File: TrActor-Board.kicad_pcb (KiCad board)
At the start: 6 copper layers, 26 x 50 mm, 125 parts, among them J1 TagConnect, J2 Debug, J3 GCT4720, J4 Batt, J5 NTC, Q1 NMOS, SW1 Power, SW2 Reset, U1 nRF52833_QDxx, U2 DW3210, U3 ICM-40609, U4 ATX-13, U5 nPM1300, U6 USBLC6-2P6, U7 USBLC6-2P6, Y1 32MHz, Y2 32.768k

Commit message: mag added. ready for order?
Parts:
- added C46: 2.2u, Capacitor_SMD:C_0603_1608Metric, F.Cu at (147.1, 99.1)
- added U8: MMC5603NJ, Package_BGA:WLP-4_0.86x0.86mm_P0.4mm, F.Cu at (150.0, 98.5)
- R7, R8: value 10k -> 2.7k
- moved TP29 0.28 mm to (151.5, 83.0)
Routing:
- net SDA: track 23.0 -> 26.1 mm, vias 2 -> 3
- net /BATT_RAW: track 12.7 -> 15.5 mm
- net SCL: track 22.7 -> 25.2 mm, vias 2 -> 3
- net +1V8: track 49.1 -> 50.4 mm, vias 16 -> 18
- net VSYS: track 75.4 -> 76.0 mm
- net GND: track 162.3 -> 162.0 mm, vias 70 -> 134
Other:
- outline, holes or cut-outs redrawn
- board text added: "1V8"
- board text added: "2V5"
- board text added: "BATT"
- board text added: "Batt+"
- board text added: "DW"
- board text added: "Designed by: Nic DeBruin Project TrActor WPI ECE MQP 2026"
- board text added: "EXTON"
- board text added: "GND"
- board text added: "Git Hash: @{vcsidentifier(7)}"
- board text added: "IMU"
- board text added: "INT1-2"
- board text added: "IRQ"
- board text added: "MISO"
- board text added: "MOSI"
- board text added: "NTC+"
- board text added: "PWR"
- board text added: "RST"
- board text added: "RX"
- board text added: "SCL"
- board text added: "SDA"
- board text added: "SYNC"
- board text added: "TO:DO: - funny silkscreen - version tracking - JLCPCB serial number thing"
- board text added: "TX"
- board text added: "TrActor."
- board text added: "VBUS"
- board text added: "VPRE"
- board text added: "VSYS"
- board text added: "WAKE"
- board text removed: "#are we actually using these lol?"
- board text removed: "PLACEHOLDER, THIS THING IS ASS"
- board text removed: "TO:DO: - Figure out actually good NFC antenna & place - layout nPM - finalize LED positions - locate test points & tagconnect on back of board - decide on side for programming header (probably front?)"

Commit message: ordering commit fr
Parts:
- FB1: footprint Inductor_SMD:L_0603_1608Metric -> Inductor_SMD:L_0402_1005Metric
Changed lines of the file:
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@@
 			)
 		)
-		(attr smd dnp)
+		(attr smd exclude_from_bom dnp)
 		(duplicate_pad_numbers_are_jumpers no)
 		(fp_rect
@@
 			)
 		)
-		(attr smd dnp)
+		(attr smd exclude_from_bom dnp)
 		(duplicate_pad_numbers_are_jumpers no)
 		(fp_rect
@@
 		)
 	)
-	(footprint "Inductor_SMD:L_0603_1608Metric"
+	(footprint "Inductor_SMD:L_0402_1005Metric"
 		(layer "F.Cu")
 		(at 139.85 87.22 90)
-		(descr "Inductor SMD 0603 (1608 Metric), square (rectangular) end terminal, IPC-7351 nominal, (Body size source: http://www.tortai-tech.com/upload/download/2011102023233369053.pdf)")
+		(descr "Inductor SMD 0402 (1005 Metric), square (rectangular) end terminal, IPC-7351 nominal, (Body size source: http://www.tortai-tech.com/upload/download/2011102023233369053.pdf)")
 		(tags "inductor")
 		(property "Reference" "FB1"
-			(at 0 -1.43 90)
+			(at 0 -1.17 90)
 			(layer "F.SilkS")
 			(hide yes)
@@
 		)
 		(property "Value" "BLM15PX330SZ1D"
-			(at 0 1.43 90)
+			(at 0 1.17 90)
 			(layer "F.Fab")
 			(effects
@@
 		(attr smd)
 		(duplicate_pad_numbers_are_jumpers no)
-		(fp_line
-			(start -0.162779 -0.51)
-			(end 0.162779 -0.51)
-			(stroke
-				(width 0.12)
-				(type solid)
-			)
-			(layer "F.SilkS")
-		)
-		(fp_line
-			(start -0.162779 0.51)
-			(end 0.162779 0.51)
-			(stroke
-				(width 0.12)
-				(type solid)
-			)
-			(layer "F.SilkS")
-		)
 		(fp_rect
-			(start -1.48 -0.73)
-			(end 1.48 0.73)
+			(start -0.93 -0.47)
+			(end 0.93 0.47)
 			(stroke
 				(width 0.05)
@@
 		)
 		(fp_rect
-			(start -0.8 -0.4)
-			(end 0.8 0.4)
+			(start -0.5 -0.25)
+			(end 0.5 0.25)
 			(stroke
 				(width 0.1)
@@
 			(effects
 				(font
-					(size 0.4 0.4)
-					(thickness 0.06)
+					(size 0.25 0.25)
+					(thickness 0.04)
 				)
 			)
 		)
 		(pad "1" smd roundrect
-			(at -0.7875 0 90)
-			(size 0.875 0.95)
+			(at -0.485 0 90)
+			(size 0.59 0.64)
 			(layers "F.Cu" "F.Mask" "F.Paste")
 			(roundrect_rratio 0.25)
@@
 		)
 		(pad "2" smd roundrect
-			(at 0.7875 0 90)
-			(size 0.875 0.95)
+			(at 0.485 0 90)
+			(size 0.59 0.64)
 			(layers "F.Cu" "F.Mask" "F.Paste")
 			(roundrect_rratio 0.25)
@@
 		)
 		(embedded_fonts no)
-		(model "${KICAD10_3DMODEL_DIR}/Inductor_SMD.3dshapes/L_0603_1608Metric.step"
+		(model "${KICAD10_3DMODEL_DIR}/Inductor_SMD.3dshapes/L_0402_1005Metric.step"
 			(offset
 				(xyz 0 0 0)
@@
 			)
 		)
+		(attr exclude_from_bom)
 		(duplicate_pad_numbers_are_jumpers no)
 		(fp_line
@@
 			)
 		)
+		(attr exclude_from_bom)
 		(duplicate_pad_numbers_are_jumpers no)
 		(fp_circle
@@
 			)
 		)
+		(attr exclude_from_bom)
 		(duplicate_pad_numbers_are_jumpers no)
 		(fp_line
@@
 			)
 		)
+		(attr exclude_from_bom)
 		(duplicate_pad_numbers_are_jumpers no)
 		(fp_circle
@@
 			)
 		)
+		(attr exclude_from_bom)
 		(duplicate_pad_numbers_are_jumpers no)
 		(fp_circle
@@
 			)
 		)
+		(attr exclude_from_bom)
 		(duplicate_pad_numbers_are_jumpers no)
 		(fp_line
@@
 			)
 		)
+		(attr exclude_from_bom)
 		(duplicate_pad_numbers_are_jumpers no)
 		(fp_circle
@@
 			)
 		)
+		(attr exclude_from_bom)
 		(duplicate_pad_numbers_are_jumpers no)
 		(fp_line
@@
 			)
 		)
+		(attr exclude_from_bom)
 		(duplicate_pad_numbers_are_jumpers no)
 		(fp_circle
@@
 			)
 		)
+		(attr exclude_from_bom)
 		(duplicate_pad_numbers_are_jumpers no)
 		(fp_circle
@@
 			)
 		)
+		(attr exclude_from_bom)
 		(duplicate_pad_numbers_are_jumpers no)
 		(fp_circle
@@
 			)
 		)
+		(attr exclude_from_bom)
 		(duplicate_pad_numbers_are_jumpers no)
 		(fp_circle
@@
 			)
 		)
+		(attr exclude_from_bom)
 		(duplicate_pad_numbers_are_jumpers no)
 		(fp_line
@@
 			)
 		)
+		(attr exclude_from_bom)
 		(duplicate_pad_numbers_are_jumpers no)
 		(fp_circle
@@
 			)
 		)
+		(attr exclude_from_bom)
 		(duplicate_pad_numbers_are_jumpers no)
 		(fp_circle
@@
 			)
 		)
+		(attr exclude_from_bom)
 		(duplicate_pad_numbers_are_jumpers no)
 		(fp_circle
@@
 			)
 		)
+		(attr exclude_from_bom)
 		(duplicate_pad_numbers_are_jumpers no)
 		(fp_circle
@@
 			)
 		)
+		(attr exclude_from_bom)
 		(duplicate_pad_numbers_are_jumpers no)
 		(fp_circle
@@
 			)
 		)
+		(attr exclude_from_bom)
 		(duplicate_pad_numbers_are_jumpers no)
 		(fp_line
@@
 			)
 		)
+		(attr exclude_from_bom)
 		(duplicate_pad_numbers_are_jumpers no)
 		(fp_circle
@@
 			)
 		)
+		(attr exclude_from_bom)
 		(duplicate_pad_numbers_are_jumpers no)
 		(fp_circle
@@
 			)
 		)
+		(attr exclude_from_bom)
 		(duplicate_pad_numbers_are_jumpers no)
 		(fp_circle
@@
 			)
 		)
+		(attr exclude_from_bom)
 		(duplicate_pad_numbers_are_jumpers no)
 		(fp_circle
@@
 			)
 		)
+		(attr exclude_from_bom)
 		(duplicate_pad_numbers_are_jumpers no)
 		(fp_circle
@@
 			)
 		)
+		(attr exclude_from_bom)
 		(duplicate_pad_numbers_are_jumpers no)
 		(fp_line

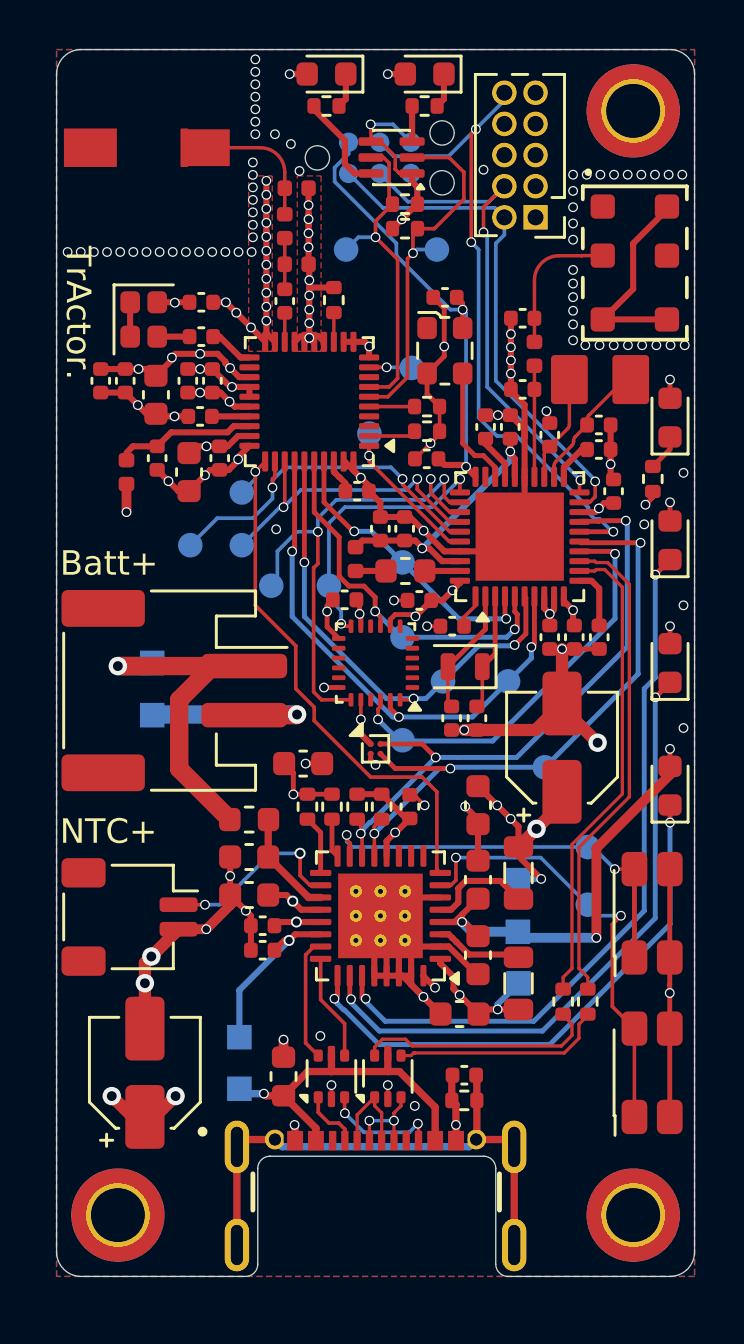
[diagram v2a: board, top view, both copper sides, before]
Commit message: ordering but the vias aren't fake
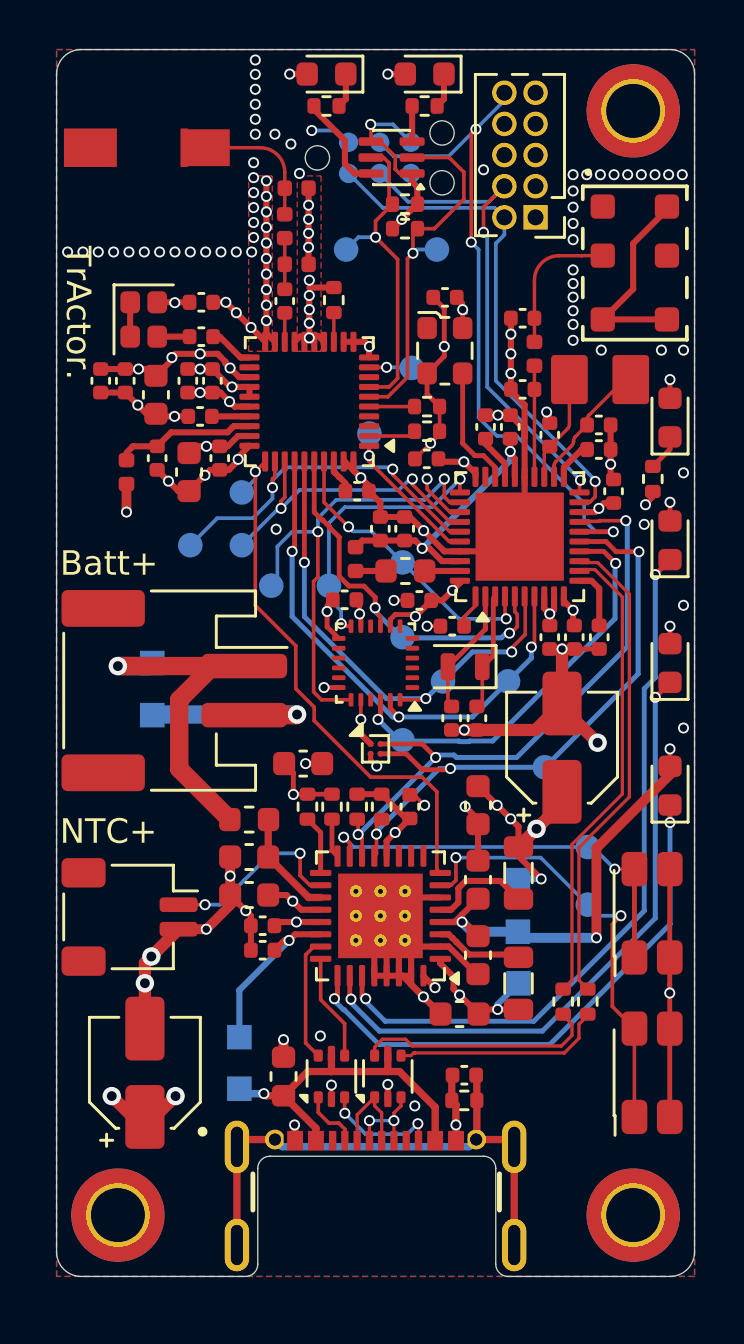
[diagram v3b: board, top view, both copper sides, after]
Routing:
- net +1V8: track 50.4 -> 36.4 mm, vias 18 -> 19
- net GND: track 162.0 -> 160.7 mm, vias 134 -> 123
- net SCL: track 25.2 -> 25.9 mm
- net MOSI: track 19.9 -> 20.5 mm
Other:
- board text added: "TO:DO: - fix vias?"
- board text removed: "TO:DO: - funny silkscreen - version tracking - JLCPCB serial number thing"
